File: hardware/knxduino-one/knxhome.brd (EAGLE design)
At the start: 38.9 x 38.9 mm, 40 parts, among them U1 AP2114H-3.3TRG1, U2 STM32F334K8T6

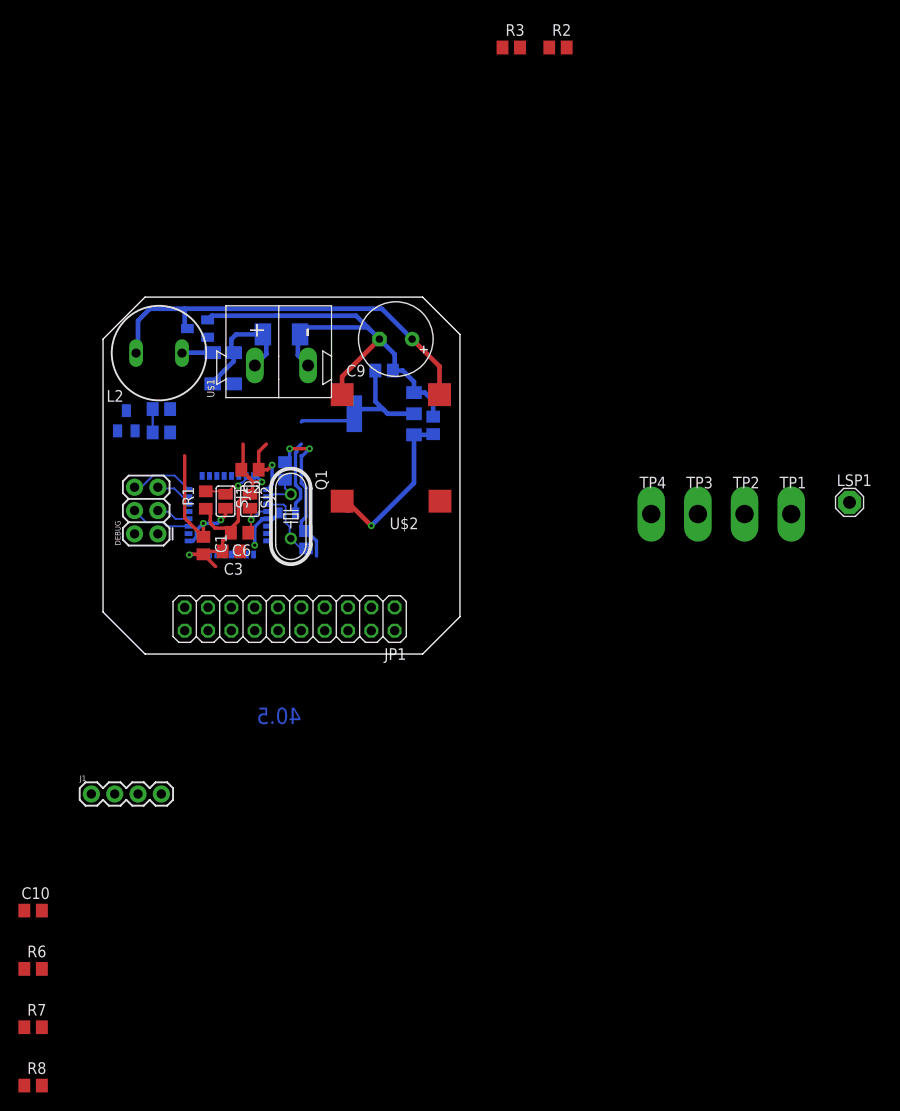
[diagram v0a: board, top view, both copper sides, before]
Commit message: Switching to STM32L4 LQFP48, new TX and RX design
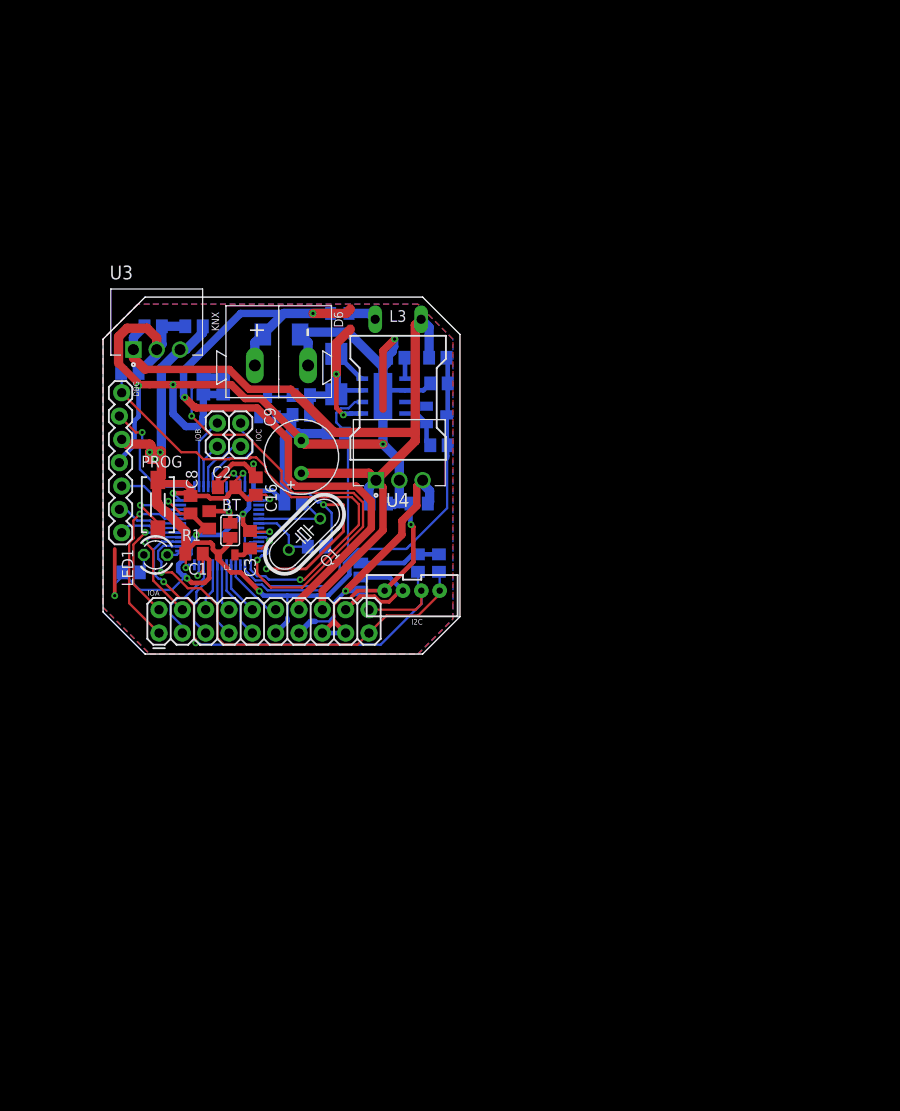
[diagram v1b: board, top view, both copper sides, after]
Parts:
- removed D12: 1N4148, diode:MINIMELF
- removed D3: BZX84C33, diode:SOT23
- removed DEBUG: (no value), SparkFun-Connectors:2X3
- removed J1: (no value), SparkFun-Connectors:1X04
- removed JP1: (no value), pinhead:2X10
- removed L2: 150mH, inductor-neosid:BS11
- removed LSP1: SE14, solpad:SE14
- removed SJ1, SJ2: (no value), jumper:SJ
- removed TP1, TP2, TP3, TP4: TPSQPAD1-20Y, testpad:P1-20Y
- removed U1: AP2114H-3.3TRG1, ics:SOT-223-WAVE
- removed U2: STM32F334K8T6, micro-stm_v3:LQFP32
- added BT: (no value), jumper:SJ
- added C11, C14, C15: 10u, rcl:C0805
- added C12, C16: 100n, rcl:C0805
- added C13: 10n, rcl:C0805
- added D4: 3V3, diode:SOT23
- added D5: 7V5@400mA, diode:SMB
- added D6: 400mA, zetex:SOD323
- added DBG: (no value), SparkFun-Connectors:1X07_LOCK
- added I2C: (no value), SparkFun-Connectors:JST-4-PTH-VERT
- added I2C_U: (no value), jumper:SJ_2
- added IC1: STM32L431CCT, micro-stm_v3:LQFP48
- added IOA: (no value), SparkFun-Connectors:2X10
- added IOB, IOC: (no value), SparkFun-Connectors:1X02
- added L3: 150mH, inductor-neosid:BS11_LIEGEND
- added LED1: (no value), led:LED3MM
- added PROG: DTSM-3, switch-tact:DTSM-3
- added R10: 510R, rcl:R0805
- added R9: 1k, rcl:R0805
- added U3: VXO7803-500, VXO7803-500:CONV_VXO7803-500
- added U4: VXO7805-500, VXO7803-500:CONV_VXO7803-500
- C10: value 47n -> 10p
- C7: value 4u7 -> 10u
- C8: value 4u7 -> 100n
- D11: value 1N4148 -> TS4148; device diode:MINIMELF -> diode:D0805
- D2: value BZX84C3V3 -> 3V3
- R4: value 47k -> 33k
- R5: value 100k (NC) -> 1k
- R6: value 100k -> 0.25R
- R7: value 1k -> 100k
- R8: value 22k -> 33k
- U$2: value ROF-78E5.0-0.5SMD-R -> STCS1; device rof-78e:ROF-78EX-XSMD-R -> Synapseware:POWERSO-8
- moved R8 90.7 mm to (36.4, 32.3), flipped to the bottom
- moved R6 77.4 mm to (31.9, 32.3), flipped to the bottom, turned to 180 degrees
- moved R7 72.6 mm to (25.4, 24.0), flipped to the bottom, turned to 180 degrees
- moved C10 60.1 mm to (10.9, 29.2), flipped to the bottom, turned to 270 degrees
- moved R2 58.2 mm to (34.3, 9.91), flipped to the bottom, turned to 90 degrees
- moved R3 56.7 mm to (36.6, 9.91), flipped to the bottom, turned to 90 degrees
- moved D2 33.8 mm to (36.3, 26.0), turned to 90 degrees
- moved C8 25.6 mm to (9.53, 16.3), flipped to the top, turned to 270 degrees
- moved C6 21.1 mm to (2.92, 30.6), flipped to the bottom
- moved C9 16.4 mm to (21.6, 21.5), turned to 90 degrees
- moved R4 15.3 mm to (21.6, 28.2)
- moved D11 15.1 mm to (25.8, 37.1), turned to 0 degrees
- moved C7 8.64 mm to (34.4, 16.4), turned to 0 degrees
- moved R5 8.43 mm to (13.1, 29.2), turned to 90 degrees
- moved L1 8.03 mm to (13.5, 10.8), flipped to the top
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- renumbered U$1 to KNX
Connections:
- removed net DCDC_OUT: C7.1, U$2.VOUT, U1.P$3
- removed net EIB+: D1.C, D11.A, D12.A, KNX.1+
- removed net EIB_AC: C10.1, D12.C, R6.2
- removed net EIB_DC: C9.+, D3.3, L2.2, U$2.VIN
- removed net KNX_RX: D2.3, R4.1, R5.2, R7.1, R7.2, R8.1, U2.14
- removed net N$53: D11.C, L2.1
- removed net OSC_IN: C5.2, Q1.1, U2.2
- removed net OSC_OUT: C4.1, Q1.2, U2.3
- removed net SWO: U2.26
- removed net UART1_RX: DEBUG.3, U2.20
- removed net UART1_TX: DEBUG.4, U2.19
- new net +5V: C7.1, I2C_U.1, IOA.13, U4.3
- new net DRX: DBG.6, IC1.31
- new net DTX: DBG.7, IC1.30
- new net I2C_VDD: I2C.3, I2C_U.2, IOA.18
- new net IO1: IC1.32, IOA.1
- new net IO10: IC1.39, IOB.2
- new net IO11: IC1.40, IOC.2
- new net IO12: IC1.41, IOC.1
- new net IO2: IC1.29, IOA.2
- new net IO3: IC1.28, IOA.4
- new net IO4: IC1.20, IOA.6
- new net IO5: IC1.18, IOA.8
- new net IO6: IC1.17, IOA.9
- new net IO7: IC1.16, IOA.10
- new net IO8: IC1.15, IOA.12
- new net IO9: IC1.38, IOB.1
- new net IO_RE: IC1.19, IOA.7
- new net IO_RX: IC1.22, IOA.3
- new net IO_TX: IC1.21, IOA.5
- new net KNX+: D1.C, D11.A, D6.2, IOA.14, KNX.1+
- new net KNX_DC: C11.1, C14.1, C9.+, IOA.16, L3.2, R8.2, U3.1, U4.1
- new net KNX_DC_AN: C13.1, D2.3, IC1.14, R8.1, R9.2
- new net KNX_RECT: C12.1, D5.C, D6.1, R4.2, U$2.1, U$2.3
- new net KNX_RX_AN: C10.1, D4.3, IC1.11, R4.1, R5.2
- new net N$3: R6.2, U$2.5
- new net N$4: LED1.K, R10.1
- new net N$5: IC1.10, IC1.12
- new net N$7: C4.1, IC1.6, Q1.1
- new net N$8: C5.2, IC1.5, Q1.2
- new net REF: D5.A, U$2.4
- net +3V3: now also BT.2, C15.1, C16.1, DBG.3, I2C_U.3, IC1.1, IC1.24, IC1.36, IC1.48, IOA.11, PROG.2, U3.3; no longer DEBUG.2, J1.2, R8.2, SJ1.2, U1.P$2, U1.P$4, U2.1, U2.17
- net BOOT0: now also BT.1, IC1.44; no longer SJ1.1, U2.31
- net BTN: now also IC1.33, PROG.1; no longer U2.15
- net GND: now also C10.2, C11.2, C12.2, C13.2, C14.2, C15.2, C16.2, D4.1, DBG.4, I2C.4, IC1.23, IC1.35, IC1.47, IC1.8, IOA.15, IOA.17, R10.2, R7.1, R9.1, U$2.6, U$2.EX, U3.2, U4.2; no longer D3.1, DEBUG.1, J1.1, SJ2.1, U$2.GND, U1.P$1, U2.16, U2.32
- net I2C_SCL: now also I2C.1, IC1.26, IOA.19; no longer J1.4, U2.29
- net I2C_SDA: now also I2C.2, IC1.27, IOA.20; no longer J1.3, U2.30
- net KNX_TX: now also IC1.13, R7.2, U$2.2; no longer U2.13
- net LED: now also IC1.25, LED1.A; no longer U2.28
- net N$1: now also D11.C, L3.1; no longer C10.2, R4.2
- net NRST: now also DBG.1, IC1.7; no longer SJ2.2, U2.4
- net SWCLK: now also DBG.2, IC1.37; no longer DEBUG.6, U2.24
- net SWDIO: now also DBG.5, IC1.34; no longer DEBUG.5, U2.23
- net VDDA: now also IC1.9; no longer U2.5
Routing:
- net GND: track 97.8 -> 276.8 mm, vias 4 -> 16
- net KNX_DC: track 0.00 -> 91.3 mm
- net KNX+: track 0.00 -> 75.4 mm, vias 0 -> 2
- net KNX_RX_AN: track 0.00 -> 61.3 mm, vias 0 -> 2
- net +3V3: track 52.3 -> 106.5 mm, vias 3 -> 8
- net I2C_SDA: track 0.00 -> 53.5 mm, vias 0 -> 2
- net NRST: track 4.96 -> 56.3 mm
- net I2C_SCL: track 0.00 -> 45.9 mm, vias 0 -> 1
- net KNX_DC_AN: track 0.00 -> 45.2 mm
- net EIB_DC: track 44.9 -> 0.00 mm
- net KNX_TX: track 0.00 -> 34.6 mm
- net +5V: track 0.00 -> 28.0 mm, vias 0 -> 1
- net KNX_RECT: track 0.00 -> 22.6 mm, vias 0 -> 2
- net IO1: track 0.00 -> 19.8 mm, vias 0 -> 1
- net DCDC_OUT: track 19.3 -> 0.00 mm, vias 1 -> 0
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- added copper zone on layer 1, net GND
- added copper zone on layer 16, net GND
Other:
- board text removed: "40.5"

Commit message: Some HW notes after first physical PCBs were made
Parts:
- C15, C7: value 10u -> 22u
- moved I2C_U 1.27 mm to (28.1, 9.65)
- renumbered C10 to C10*, C13 to C13*, D2 to D2*, D4 to D4*
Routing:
- net GND: track 276.8 -> 284.7 mm, vias 16 -> 18
- net KNX_DC_AN: track 45.2 -> 47.2 mm
- net +3V3: track 106.5 -> 107.4 mm
- net +5V: track 28.0 -> 28.5 mm
